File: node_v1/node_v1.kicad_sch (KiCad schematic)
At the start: 33 parts, among them J1 Conn_Coaxial, J10 Conn_01x02_Pin, J11 Conn_01x04_Pin, J2 Conn_01x02_Pin, J3 Conn_01x02_Pin, J4 Micro_SD_Card, J5 Conn_01x03_Pin, J6 Conn_01x04_Pin, J7 Conn_01x06_Pin, J8 Conn_01x02_Pin, J9 Conn_01x02_Pin, Q1 2N3904, U1 Pico, U2 RFM69HCW, U3 ADP2108AUJ-3.3, U4 CAT3200-5, U5 MCP73831-2-OT

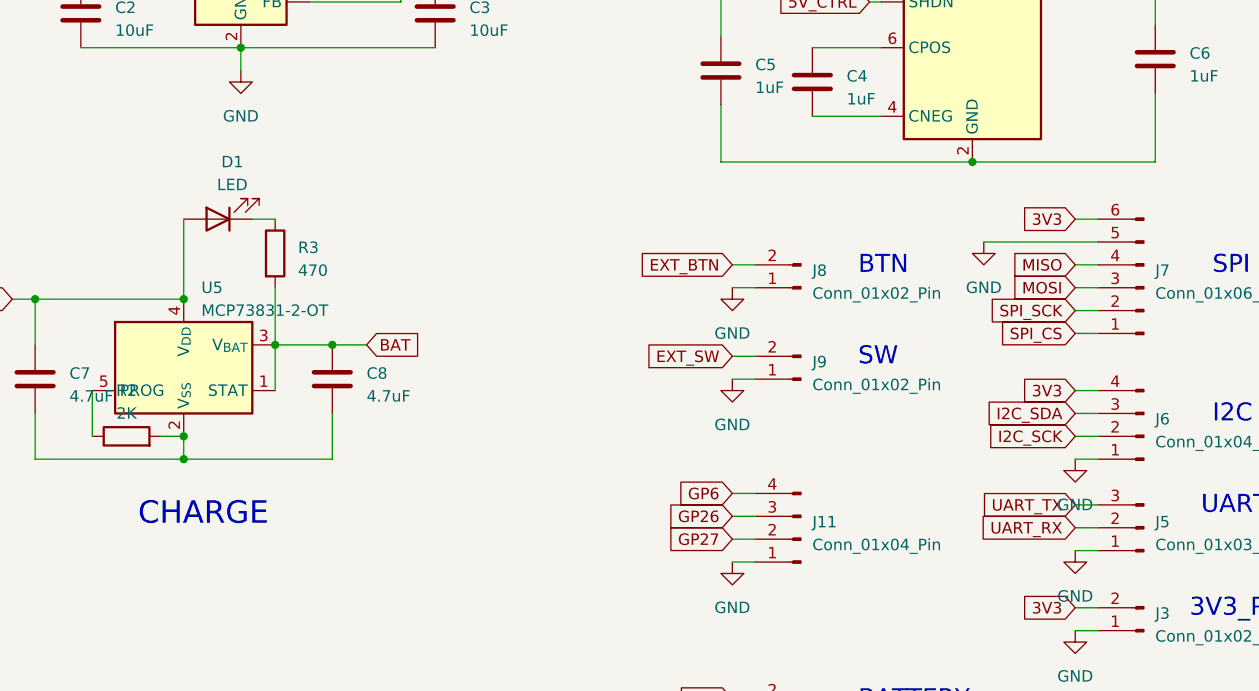
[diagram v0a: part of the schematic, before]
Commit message: moved stuff around, replaced headers, usb, footprints, started pcb
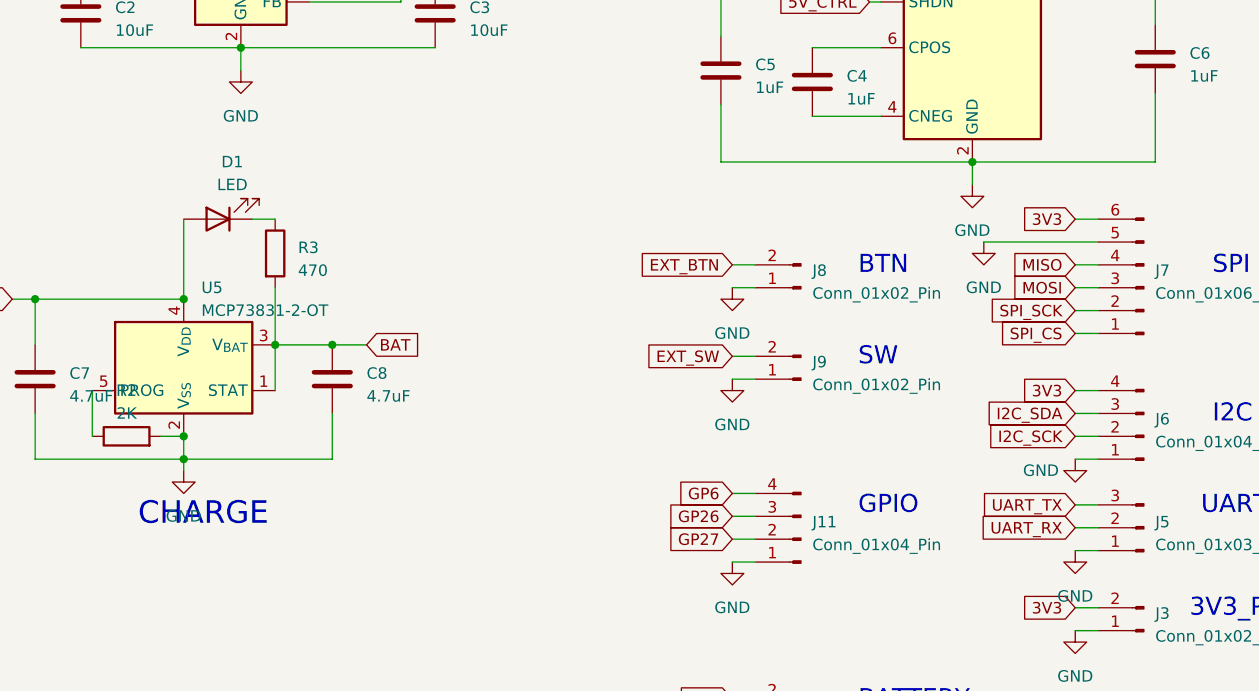
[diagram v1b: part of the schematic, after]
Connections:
- net GND: now also C5.2, C6.2, C7.2, C8.2, R2.2, U4.2 (GND), U5.2 (V_{SS})
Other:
- note added: "GPIO"
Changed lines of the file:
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@@
+    (stroke (width 0) (type default))
+  )
+  (wire (pts (xy 234.95 64.77) (xy 234.95 67.31))
     (stroke (width 0) (type default))
   )
@@
   )
   (wire (pts (xy 72.39 144.78) (xy 82.55 144.78))
+    (stroke (width 0) (type default))
+  )
+  (wire (pts (xy 147.32 97.79) (xy 147.32 99.06))
     (stroke (width 0) (type default))
   )
@@
   )
   (text "BATTERY" (at 222.25 125.73 0)
+    (effects (font (size 2 2)) (justify left bottom))
+  )
+  (text "GPIO" (at 222.25 104.14 0)
     (effects (font (size 2 2)) (justify left bottom))
   )
@@
     )
   )
+  (symbol (lib_id "power:GND") (at 147.32 99.06 0) (unit 1)
+    (in_bom yes) (on_board yes) (dnp no) (fields_autoplaced)
+    (property "Reference" "#PWR019" (at 147.32 105.41 0)
+      (effects (font (size 1.27 1.27)) hide)
+    )
+    (property "Value" "GND" (at 147.32 104.14 0)
+      (effects (font (size 1.27 1.27)))
+    )
+    (property "Footprint" "" (at 147.32 99.06 0)
+      (effects (font (size 1.27 1.27)) hide)
+    )
+    (property "Datasheet" "" (at 147.32 99.06 0)
+      (effects (font (size 1.27 1.27)) hide)
+    )
+    (pin "1")
+    (instances
+      (project "node_v1"
+        (path "/d14db98a-ceed-46e8-b675-d2a5aebf85dc"
+          (reference "#PWR019") (unit 1)
+        )
+      )
+    )
+  )
   (symbol (lib_id "power:GND") (at 22.86 166.37 0) (unit 1)
     (in_bom yes) (on_board yes) (dnp no) (fields_autoplaced)
@@
   )
   (symbol (lib_id "power:GND") (at 246.38 97.79 0) (unit 1)
-    (in_bom yes) (on_board yes) (dnp no) (fields_autoplaced)
+    (in_bom yes) (on_board yes) (dnp no)
     (property "Reference" "#PWR010" (at 246.38 104.14 0)
       (effects (font (size 1.27 1.27)) hide)
     )
-    (property "Value" "GND" (at 246.38 102.87 0)
+    (property "Value" "GND" (at 242.57 99.06 0)
       (effects (font (size 1.27 1.27)))
     )
@@
         )
       )
+    )
+  )
+  (symbol (lib_id "power:GND") (at 234.95 67.31 0) (unit 1)
+    (in_bom yes) (on_board yes) (dnp no) (fields_autoplaced)
+    (property "Reference" "#PWR018" (at 234.95 73.66 0)
+      (effects (font (size 1.27 1.27)) hide)
+    )
+    (property "Value" "GND" (at 234.95 72.39 0)
+      (effects (font (size 1.27 1.27)))
+    )
+    (property "Footprint" "" (at 234.95 67.31 0)
+      (effects (font (size 1.27 1.27)) hide)
+    )
+    (property "Datasheet" "" (at 234.95 67.31 0)
+      (effects (font (size 1.27 1.27)) hide)
+    )
+    (pin "1")
+    (instances
+      (project "node_v1"
+        (path "/d14db98a-ceed-46e8-b675-d2a5aebf85dc"
+          (reference "#PWR018") (unit 1)
+        )
+      )
